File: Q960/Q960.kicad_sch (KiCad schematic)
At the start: 11 parts, among them J101 BAT(3V), J102 BAT(3V), SW101 TS-06104, U101 SeeeduinoXIAO, U102 S-2110A, U103 S-2110A

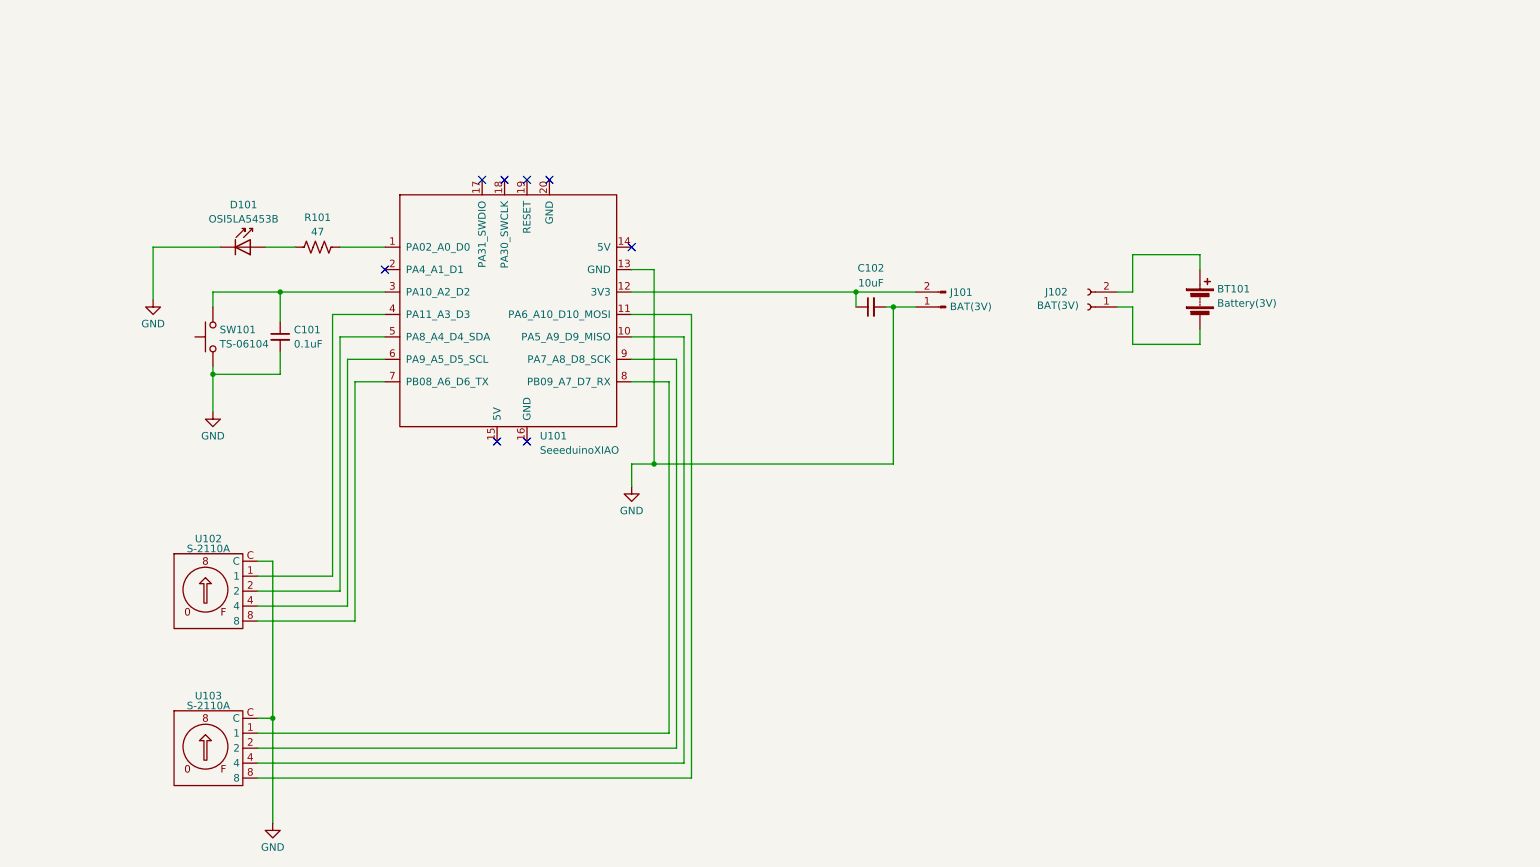
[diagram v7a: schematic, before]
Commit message: LEDにTrドライバを加える途中
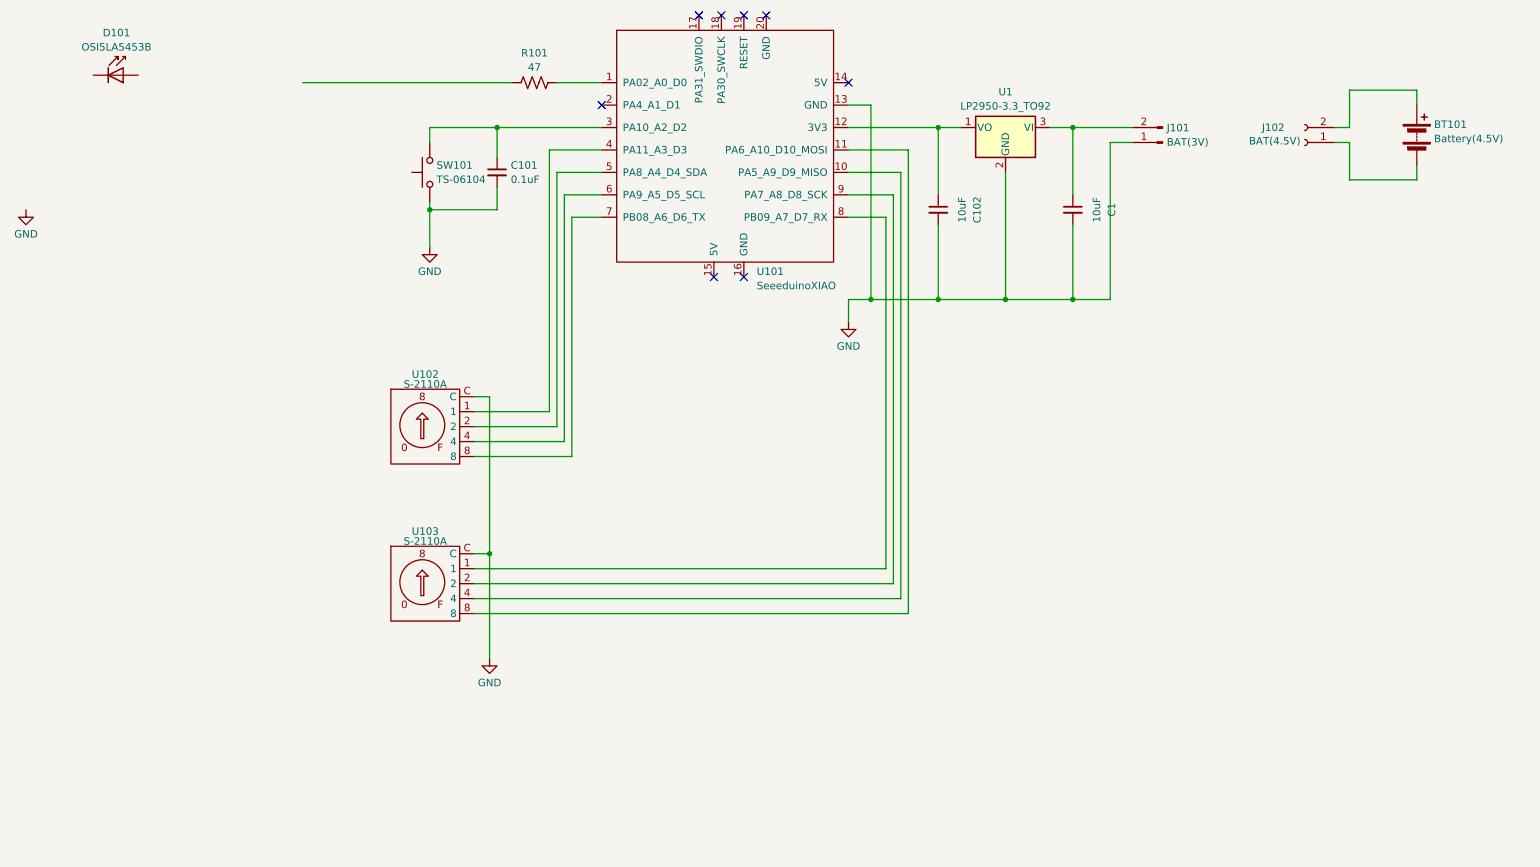
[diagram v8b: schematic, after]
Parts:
- added C1: 10uF, Capacitor_SMD:C_0805_2012Metric_Pad1.18x1.45mm_HandSolder, symbol Device:C_Small
- added U1: LP2950-3.3_TO92, Package_TO_SOT_THT:TO-92_Inline, symbol Regulator_Linear:LP2950-3.3_TO92
- BT101: value Battery(3V) -> Battery(4.5V)
- J102: value BAT(3V) -> BAT(4.5V)
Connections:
- net GND: now also C1.2, U1.2 (GND); no longer D101.1 (K)
- net at C102.1, U101.12 (3V3): now also U1.1 (VO); no longer J101.2 (Pin_2)
- net at R101.1: no longer D101.2 (A)
- new net: C1.1, J101.2 (Pin_2), U1.3 (VI)
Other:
- moved on the sheet: BT101, C101, C102, D101, J101, J102, R101, SW101, U101, U102, U103
